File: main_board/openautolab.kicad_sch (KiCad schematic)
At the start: 30 parts, among them IC1 ULN2065B, IC3 ULN2065B, J1 PIN8, J10 FILTER_PUMP, J11 FILTER_SENSOR, J12 PWR_IN, J13 HX711, J14 SERVO, J15 LCD, J2 PIN9, J3 PIN10, J4 PIN11, J5 PIN7, J6 PIN6, J7 PIN5, J8 PINA0, J9 PUMP, SW0 PIN_A3, SW1 PIN_A2, SW2 PIN_A1, SW3 SW_DPST_x2, SW4 SW_DPST_x2, U2 LM2575-5.0BT

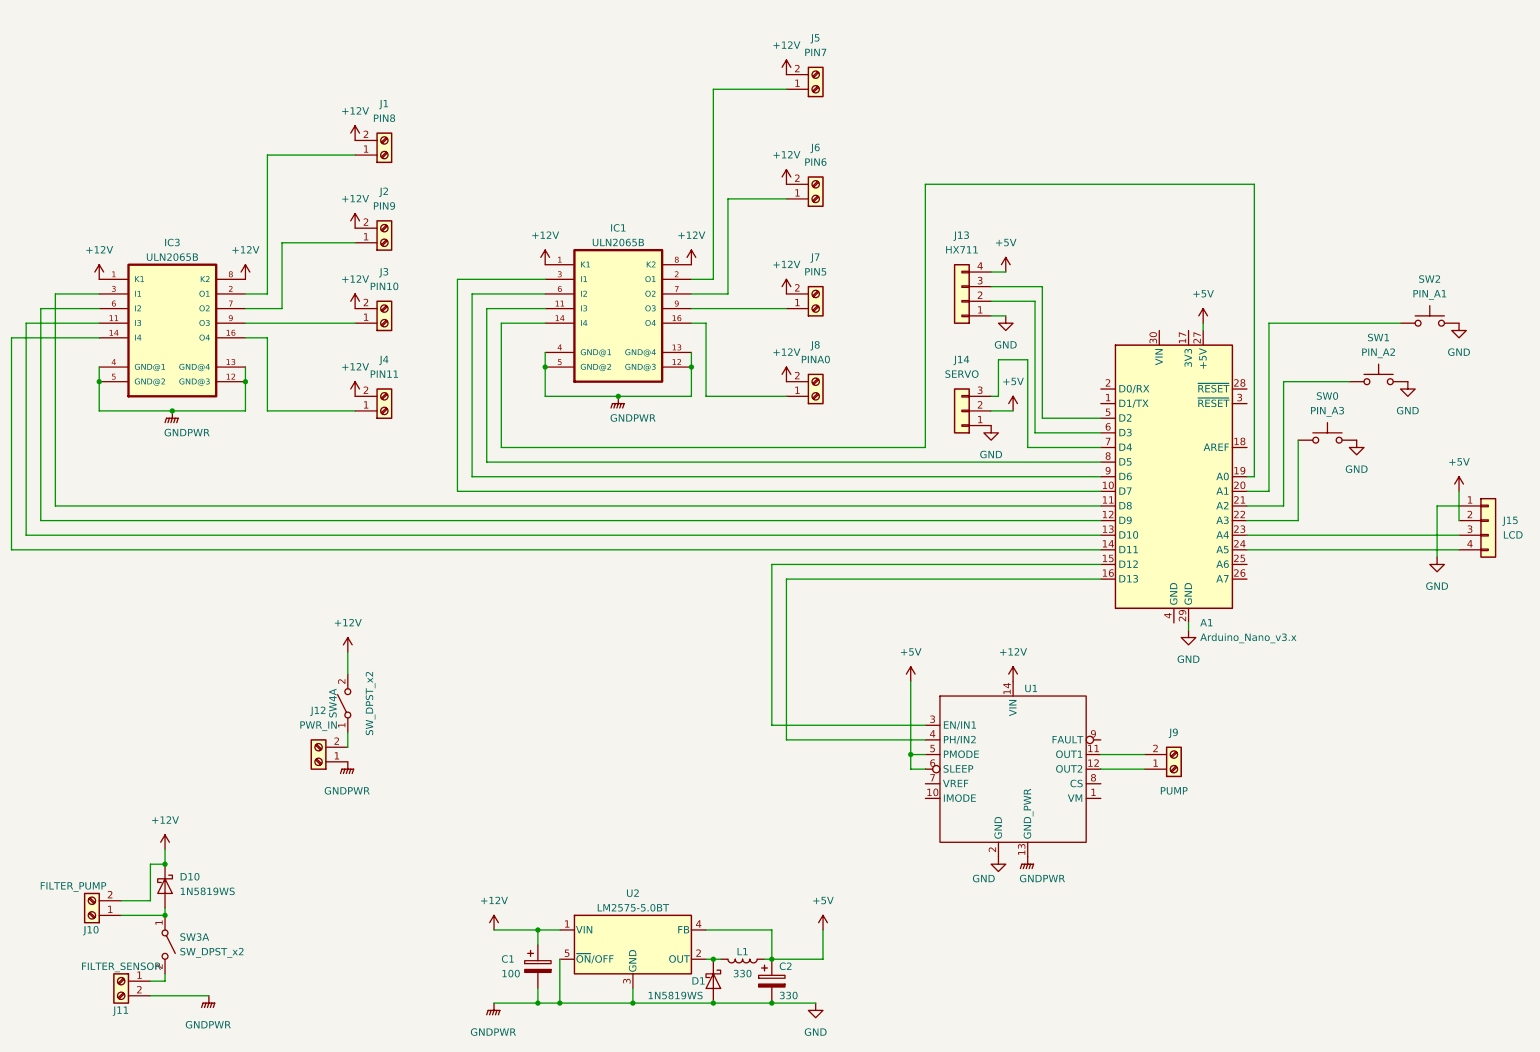
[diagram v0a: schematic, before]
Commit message: update schematic
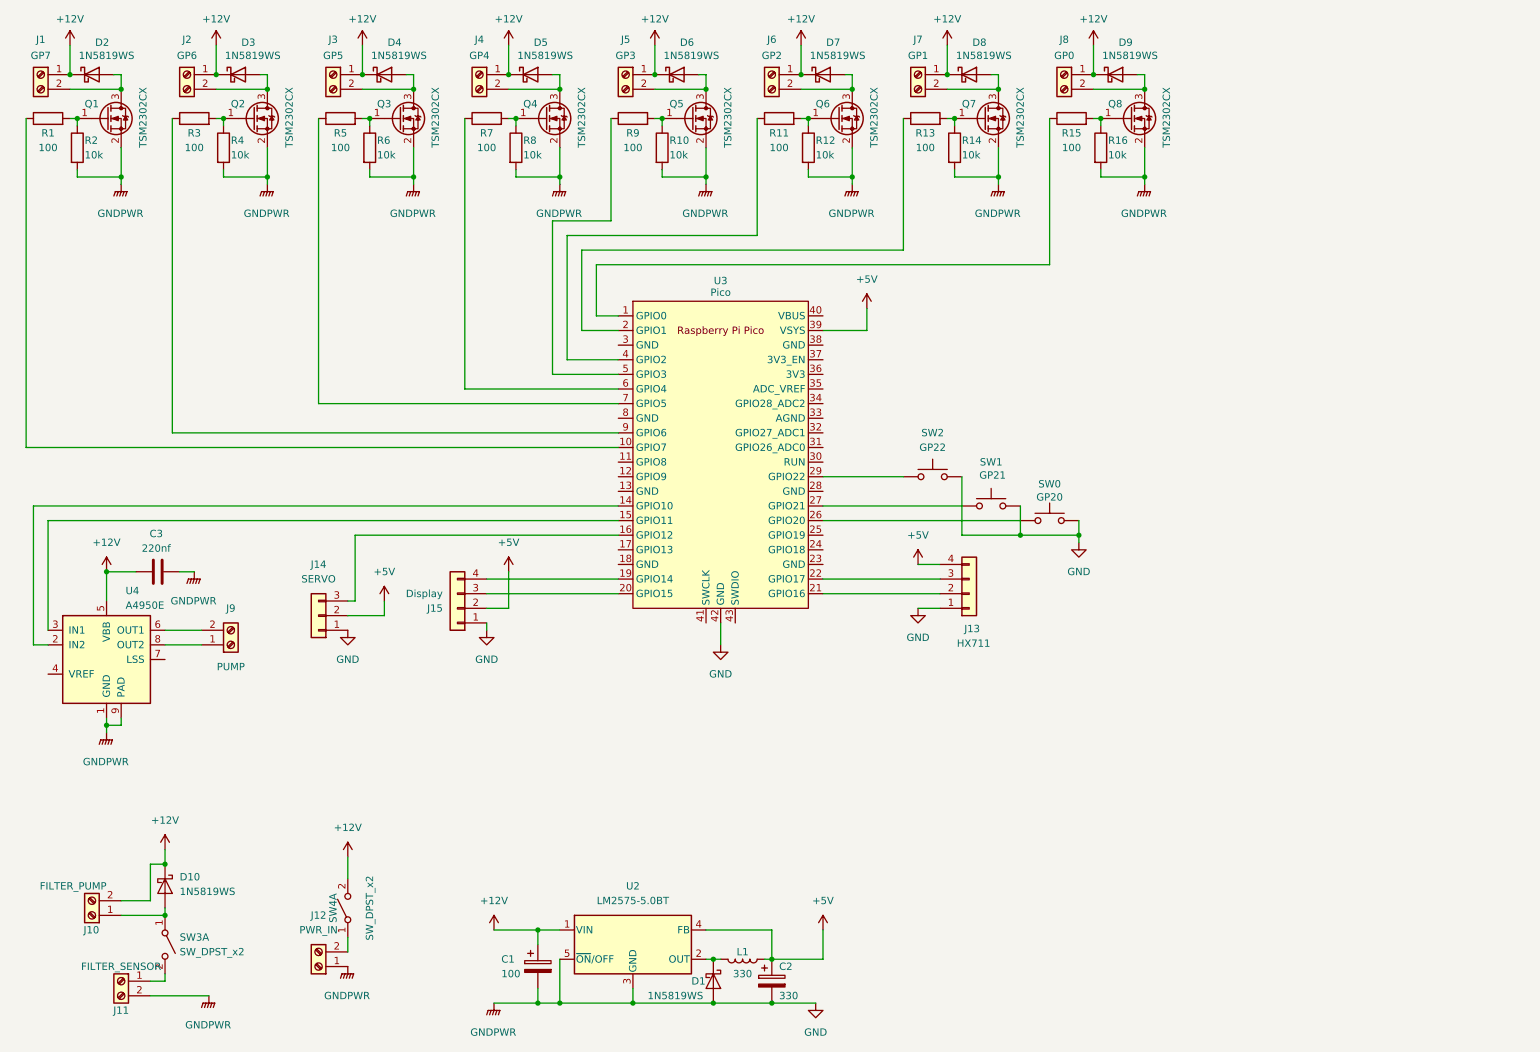
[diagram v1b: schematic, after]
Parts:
- removed A1: Arduino_Nano_v3.x, Module:Arduino_Nano, symbol MCU_Module:Arduino_Nano_v3.x
- removed IC1, IC3: ULN2065B, Package_DIP:DIP-16_W7.62mm, symbol ULN2065B:ULN2065B
- removed U1: ~, Pololu_breakout_DRV8874:Pololu_breakout_DRV8874, symbol Pololu_breakout_DRV8874:Pololu_breakout_DRV8874
- added C3: 220nf, Capacitor_SMD:C_0805_2012Metric, symbol Device:C
- added D2, D3, D4, D5, D6, D7, D8, D9: 1N5819WS, Diode_SMD:D_SOD-323, symbol Diode:1N5819WS
- added Q1, Q2, Q3, Q4, Q5, Q6, Q7, Q8: TSM2302CX, Package_TO_SOT_SMD:SOT-23, symbol Transistor_FET:TSM2302CX
- added R1, R11, R13, R15, R3, R5, R7, R9: 100, Resistor_SMD:R_0603_1608Metric, symbol Device:R
- added R10, R12, R14, R16, R2, R4, R6, R8: 10k, Resistor_SMD:R_0603_1608Metric, symbol Device:R
- added U3: Pico, dev:RPi_Pico_SMD_TH, symbol MCU_RaspberryPi_and_Boards:Pico
- added U4: A4950E, Package_SO:SOIC-8-1EP_3.9x4.9mm_P1.27mm_EP2.41x3.3mm, symbol Driver_Motor:A4950E
- J1: value PIN8 -> GP7
- J15: value LCD -> Display
- J2: value PIN9 -> GP6
- J3: value PIN10 -> GP5
- J4: value PIN11 -> GP4
- J5: value PIN7 -> GP3
- J6: value PIN6 -> GP2
- J7: value PIN5 -> GP1
- J8: value PINA0 -> GP0
- SW0: value PIN_A3 -> GP20
- SW1: value PIN_A2 -> GP21
- SW2: value PIN_A1 -> GP22
- U2: footprint Package_TO_SOT_THT:TO-220-5_P3.4x3.7mm_StaggerOdd_Lead3.8mm_Vertical -> Package_TO_SOT_SMD:TO-263-5_TabPin3
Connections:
- net +12V: now also J1.1 (Pin_1), J2.1 (Pin_1), J3.1 (Pin_1), J4.1 (Pin_1), J5.1 (Pin_1), J6.1 (Pin_1), J7.1 (Pin_1), J8.1 (Pin_1), C3.1, D2.1 (K), D3.1 (K), D4.1 (K), D5.1 (K), D6.1 (K), D7.1 (K), D8.1 (K), D9.1 (K), U4.5 (VBB); no longer J1.2 (Pin_2), J2.2 (Pin_2), J3.2 (Pin_2), J4.2 (Pin_2), J5.2 (Pin_2), J6.2 (Pin_2), J7.2 (Pin_2), J8.2 (Pin_2)
- net +5V: now also U3.39 (VSYS)
- net GND: now also C3.2, Q1.2 (S), Q2.2 (S), Q3.2 (S), Q4.2 (S), Q5.2 (S), Q6.2 (S), Q7.2 (S), Q8.2 (S), R10.2, R12.2, R14.2, R16.2, R2.2, R4.2, R6.2, R8.2, U3.42 (GND), U4.1 (GND), U4.9 (PAD)
- net at J9.1 (Pin_1): now also U4.8 (OUT2)
- net at J9.2 (Pin_2): now also U4.6 (OUT1)
- net at J14.3 (Pin_3): now also U3.16 (GPIO12)
- net at SW1.1: now also U3.27 (GPIO21)
- net at J13.2 (Pin_2): now also U3.21 (GPIO16)
- net at J13.3 (Pin_3): now also U3.22 (GPIO17)
- net at J15.3 (Pin_3): now also U3.20 (GPIO15)
- net at J15.4 (Pin_4): now also U3.19 (GPIO14)
- net at SW0.1: now also U3.26 (GPIO20)
- net at SW2.1: now also U3.29 (GPIO22)
- new net: R1.1, U3.10 (GPIO7)
- new net: Q1.1 (G), R1.2, R2.1
- new net: D2.2 (A), J1.2 (Pin_2), Q1.3 (D)
- new net: D9.2 (A), J8.2 (Pin_2), Q8.3 (D)
- new net: R15.1, U3.1 (GPIO0)
- new net: Q8.1 (G), R15.2, R16.1
- new net: Q3.1 (G), R5.2, R6.1
- new net: D4.2 (A), J3.2 (Pin_2), Q3.3 (D)
- new net: Q6.1 (G), R11.2, R12.1
- new net: D7.2 (A), J6.2 (Pin_2), Q6.3 (D)
- new net: D6.2 (A), J5.2 (Pin_2), Q5.3 (D)
- new net: Q2.1 (G), R3.2, R4.1
- new net: D3.2 (A), J2.2 (Pin_2), Q2.3 (D)
- new net: D5.2 (A), J4.2 (Pin_2), Q4.3 (D)
- new net: Q7.1 (G), R13.2, R14.1
- new net: D8.2 (A), J7.2 (Pin_2), Q7.3 (D)
- new net: R3.1, U3.9 (GPIO6)
- new net: R13.1, U3.2 (GPIO1)
- new net: R7.1, U3.6 (GPIO4)
- new net: Q4.1 (G), R7.2, R8.1
- new net: R9.1, U3.5 (GPIO3)
- new net: Q5.1 (G), R10.1, R9.2
- new net: U3.14 (GPIO10), U4.2 (IN2)
- new net: U3.15 (GPIO11), U4.3 (IN1)
- new net: R11.1, U3.4 (GPIO2)
- new net: R5.1, U3.7 (GPIO5)
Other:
- moved on the sheet: J1, J12, J13, J14, J15, J9, SW0, SW1, SW2, SW4A

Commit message: all footprints correct except toggle switch
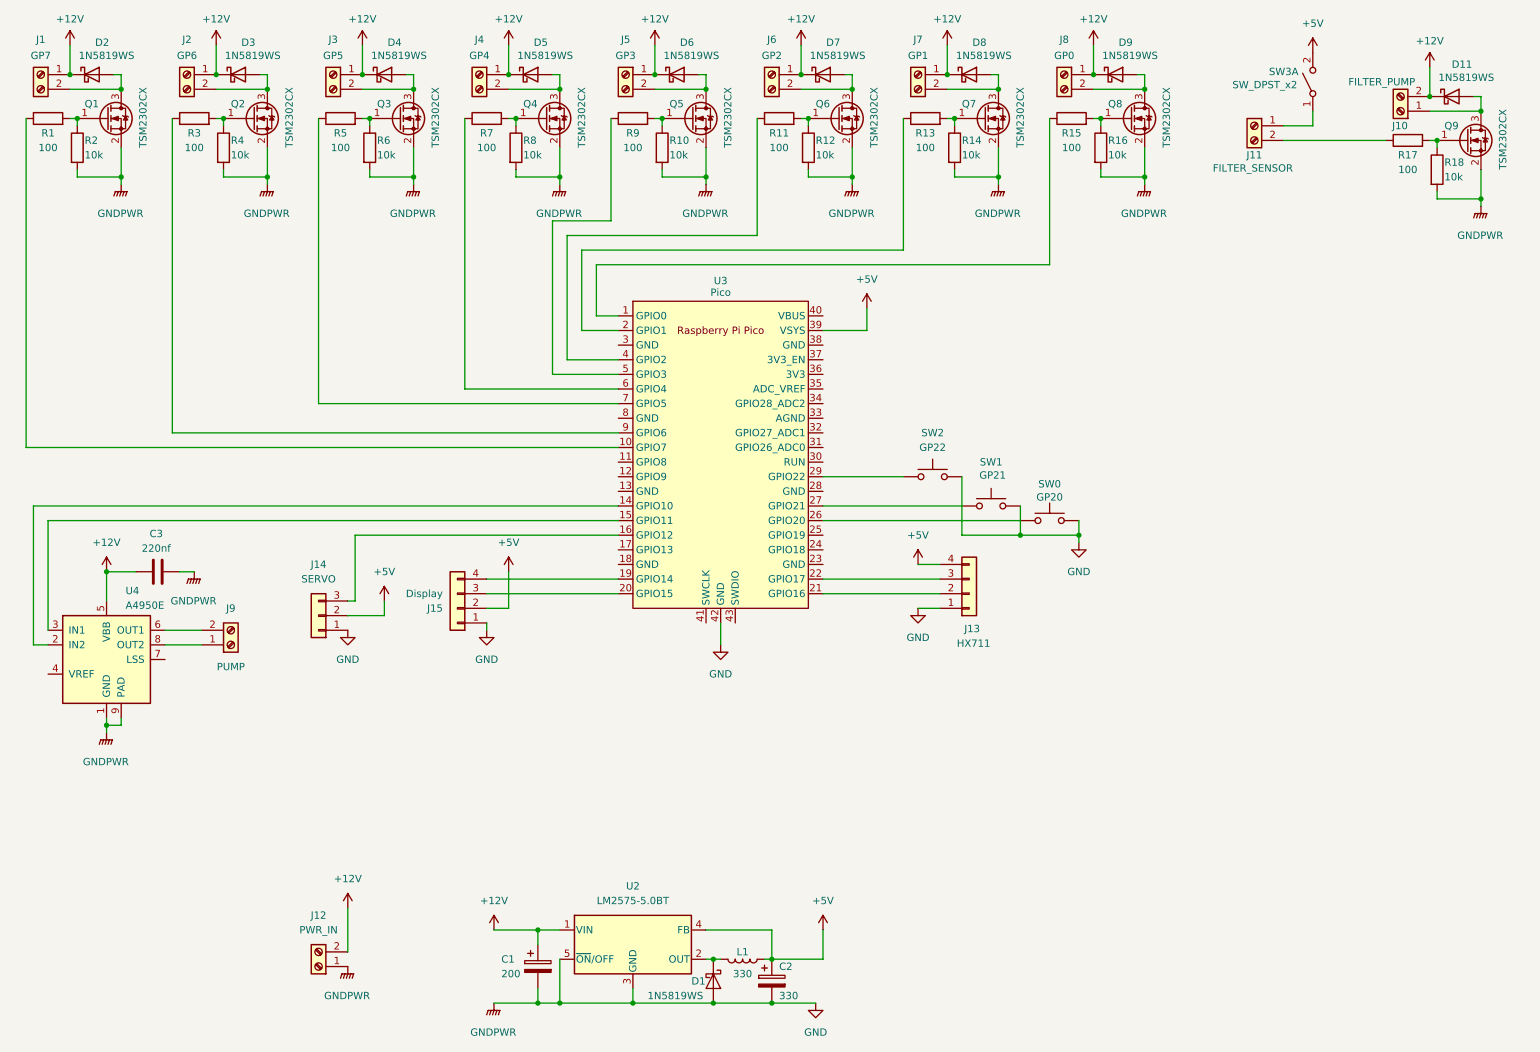
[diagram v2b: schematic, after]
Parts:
- removed D10: 1N5819WS, Diode_THT:D_A-405_P7.62mm_Horizontal, symbol Device:D_Schottky
- removed SW4: SW_DPST_x2, Connector_PinHeader_2.54mm:PinHeader_1x02_P2.54mm_Vertical, symbol Switch:SW_DPST_x2
- added D11: 1N5819WS, Diode_SMD:D_SOD-323, symbol Diode:1N5819WS
- added Q9: TSM2302CX, Package_TO_SOT_SMD:SOT-23, symbol Transistor_FET:TSM2302CX
- added R17: 100, Resistor_SMD:R_0603_1608Metric, symbol Device:R
- added R18: 10k, Resistor_SMD:R_0603_1608Metric, symbol Device:R
- C1: value 100 -> 200; footprint Capacitor_THT:CP_Radial_D8.0mm_P5.00mm -> Capacitor_SMD:CP_Elec_10x10
- C2: footprint Capacitor_THT:CP_Radial_D8.0mm_P5.00mm -> Capacitor_SMD:CP_Elec_6.3x7.7
- D1: footprint Diode_THT:D_A-405_P7.62mm_Horizontal -> Diode_SMD:D_SOD-323
- L1: footprint Inductor_THT:L_Radial_D12.0mm_P5.00mm_Fastron_11P -> Inductor_SMD:L_12x12mm_H8mm
- SW0, SW1, SW2: footprint Button_Switch_THT:SW_PUSH_6mm -> Button_Switch_SMD:SW_SPST_B3S-1000
- U3: footprint dev:RPi_Pico_SMD_TH -> RP-Pico:RPi_Pico_SMD_TH
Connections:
- net +12V: now also J12.2 (Pin_2), D11.1 (K)
- net +5V: now also SW3.2 (B)
- net GND: now also Q9.2 (S), R18.2; no longer J11.2 (Pin_2)
- net at J11.1 (Pin_1): now also SW3.1 (A); no longer SW3.2 (B)
- net at J10.1 (Pin_1): now also D11.2 (A), Q9.3 (D); no longer SW3.1 (A)
- new net: Q9.1 (G), R17.2, R18.1
- new net: J11.2 (Pin_2), R17.1

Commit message: fix footprints
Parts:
- C1: value 200 -> 200uf
- C2: value 330 -> 330uF
- C3: footprint Capacitor_SMD:C_0805_2012Metric -> Capacitor_SMD:C_0603_1608Metric
- L1: value 330 -> 330uH
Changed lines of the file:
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@@
 			)
 		)
-		(property "Footprint" "Capacitor_SMD:C_0805_2012Metric"
+		(property "Footprint" "Capacitor_SMD:C_0603_1608Metric"
 			(at 46.99 109.5248 0)
 			(effects
@@
 			)
 		)
-		(property "Value" "330"
+		(property "Value" "330uF"
 			(at 151.13 184.15 0)
 			(effects
@@
 			)
 		)
-		(property "Value" "330"
+		(property "Value" "330uH"
 			(at 144.78 180.34 90)
 			(effects
@@
 			)
 		)
-		(property "Value" "200"
-			(at 102.87 180.34 0)
+		(property "Value" "200uf"
+			(at 101.092 180.34 0)
 			(effects
 				(font

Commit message: all footprints correct. draft of a layout
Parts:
- C1: LCSC (none) -> C125977
- C2: LCSC (none) -> C7471878
- C3: footprint Capacitor_SMD:C_0603_1608Metric -> Capacitor_SMD:C_0805_2012Metric; LCSC (none) -> C5378
- L1: LCSC (none) -> C10152
- SW3: LCSC (none) -> C2941005
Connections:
- net +12V: now also J10.1 (Pin_1); no longer J10.2 (Pin_2)
- net at D11.2 (A), Q9.3 (D): now also J10.2 (Pin_2); no longer J10.1 (Pin_1)
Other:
- moved on the sheet: J10
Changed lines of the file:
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@@
 	)
 	(junction
+		(at 273.05 30.48)
+		(diameter 0)
+		(color 0 0 0 0)
+	)
+	(junction
 		(at 214.63 26.67)
 		(diameter 0)
@@
 	)
 	(junction
-		(at 264.16 27.94)
-		(diameter 0)
-		(color 0 0 0 0)
-	)
-	(junction
 		(at 139.7 185.42)
 		(diameter 0)
@@
 	)
 	(junction
+		(at 264.16 27.94)
+		(diameter 0)
+		(color 0 0 0 0)
+	)
+	(junction
 		(at 138.43 41.91)
 		(diameter 0)
@@
 	)
 	(junction
-		(at 273.05 30.48)
-		(diameter 0)
-		(color 0 0 0 0)
-	)
-	(junction
 		(at 54.61 31.75)
 		(diameter 0)
@@
 	(wire
 		(pts
-			(xy 264.16 30.48) (xy 273.05 30.48)
-		)
-		(stroke
-			(width 0)
-			(type default)
-		)
-	)
-	(wire
-		(pts
 			(xy 36.83 24.13) (xy 35.56 24.13)
 		)
@@
 	(wire
 		(pts
+			(xy 264.16 30.48) (xy 273.05 30.48)
+		)
+		(stroke
+			(width 0)
+			(type default)
+		)
+	)
+	(wire
+		(pts
 			(xy 82.55 115.57) (xy 82.55 118.11)
 		)
@@
 	(symbol
 		(lib_id "Connector:Screw_Terminal_01x02")
-		(at 259.08 30.48 180)
+		(at 259.08 27.94 0)
+		(mirror y)
 		(unit 1)
 		(exclude_from_sim no)
@@
 		(dnp no)
 		(property "Reference" "J10"
-			(at 260.35 33.02 0)
+			(at 260.35 25.4 0)
 			(effects
 				(font
@@
 		)
 		(property "Value" "FILTER_PUMP"
-			(at 261.62 25.4 0)
+			(at 261.62 33.02 0)
 			(effects
 				(font
@@
 		)
 		(property "Footprint" "TerminalBlock_Phoenix:TerminalBlock_Phoenix_MKDS-3-2-5.08_1x02_P5.08mm_Horizontal"
-			(at 259.08 30.48 0)
+			(at 259.08 27.94 0)
 			(effects
 				(font
@@
 		)
 		(property "Datasheet" "~"
-			(at 259.08 30.48 0)
+			(at 259.08 27.94 0)
 			(effects
 				(font
@@
 		)
 		(property "Description" ""
-			(at 259.08 30.48 0)
+			(at 259.08 27.94 0)
 			(effects
 				(font
@@
 			)
 		)
-		(property "Footprint" "Capacitor_SMD:C_0603_1608Metric"
+		(property "Footprint" "Capacitor_SMD:C_0805_2012Metric"
 			(at 46.99 109.5248 0)
 			(effects
@@
 			)
 		)
+		(property "LCSC" "C5378"
+			(at 153.67 153.67 0)
+			(effects
+				(font
+					(size 1.27 1.27)
+				)
+				(hide yes)
+			)
+		)
 		(pin "2"
 		)
@@
 			)
 		)
+		(property "LCSC" "C7471878"
+			(at 0 363.22 0)
+			(effects
+				(font
+					(size 1.27 1.27)
+				)
+				(hide yes)
+			)
+		)
 		(pin "1"
 		)
@@
 			)
 		)
+		(property "LCSC" "C2941005"
+			(at 269.24 269.24 0)
+			(effects
+				(font
+					(size 1.27 1.27)
+				)
+				(hide yes)
+			)
+		)
 		(pin "1"
 		)
@@
 			)
 		)
+		(property "LCSC" "C10152"
+			(at -33.02 33.02 0)
+			(effects
+				(font
+					(size 1.27 1.27)
+				)
+				(hide yes)
+			)
+		)
 		(pin "1"
 		)
@@
 			(effects
 				(font
+					(size 1.27 1.27)
+				)
+				(hide yes)
+			)
+		)
+		(property "LCSC" "C125977"
+			(at 0 358.14 0)
+			(effects
+				(font
